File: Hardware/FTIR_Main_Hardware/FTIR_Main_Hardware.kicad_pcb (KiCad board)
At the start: 2 copper layers, 63 parts, among them J1 RJ45_LED_Shielded, Q1 IRF7606PBF, Q2 BSS138, Q3 IRF7606PBF, Q4 IRF7606PBF, Q5 BSS138, Q6 BSS138, U1 Opamp_Dual, U2 D36V28F7, U3 OKI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

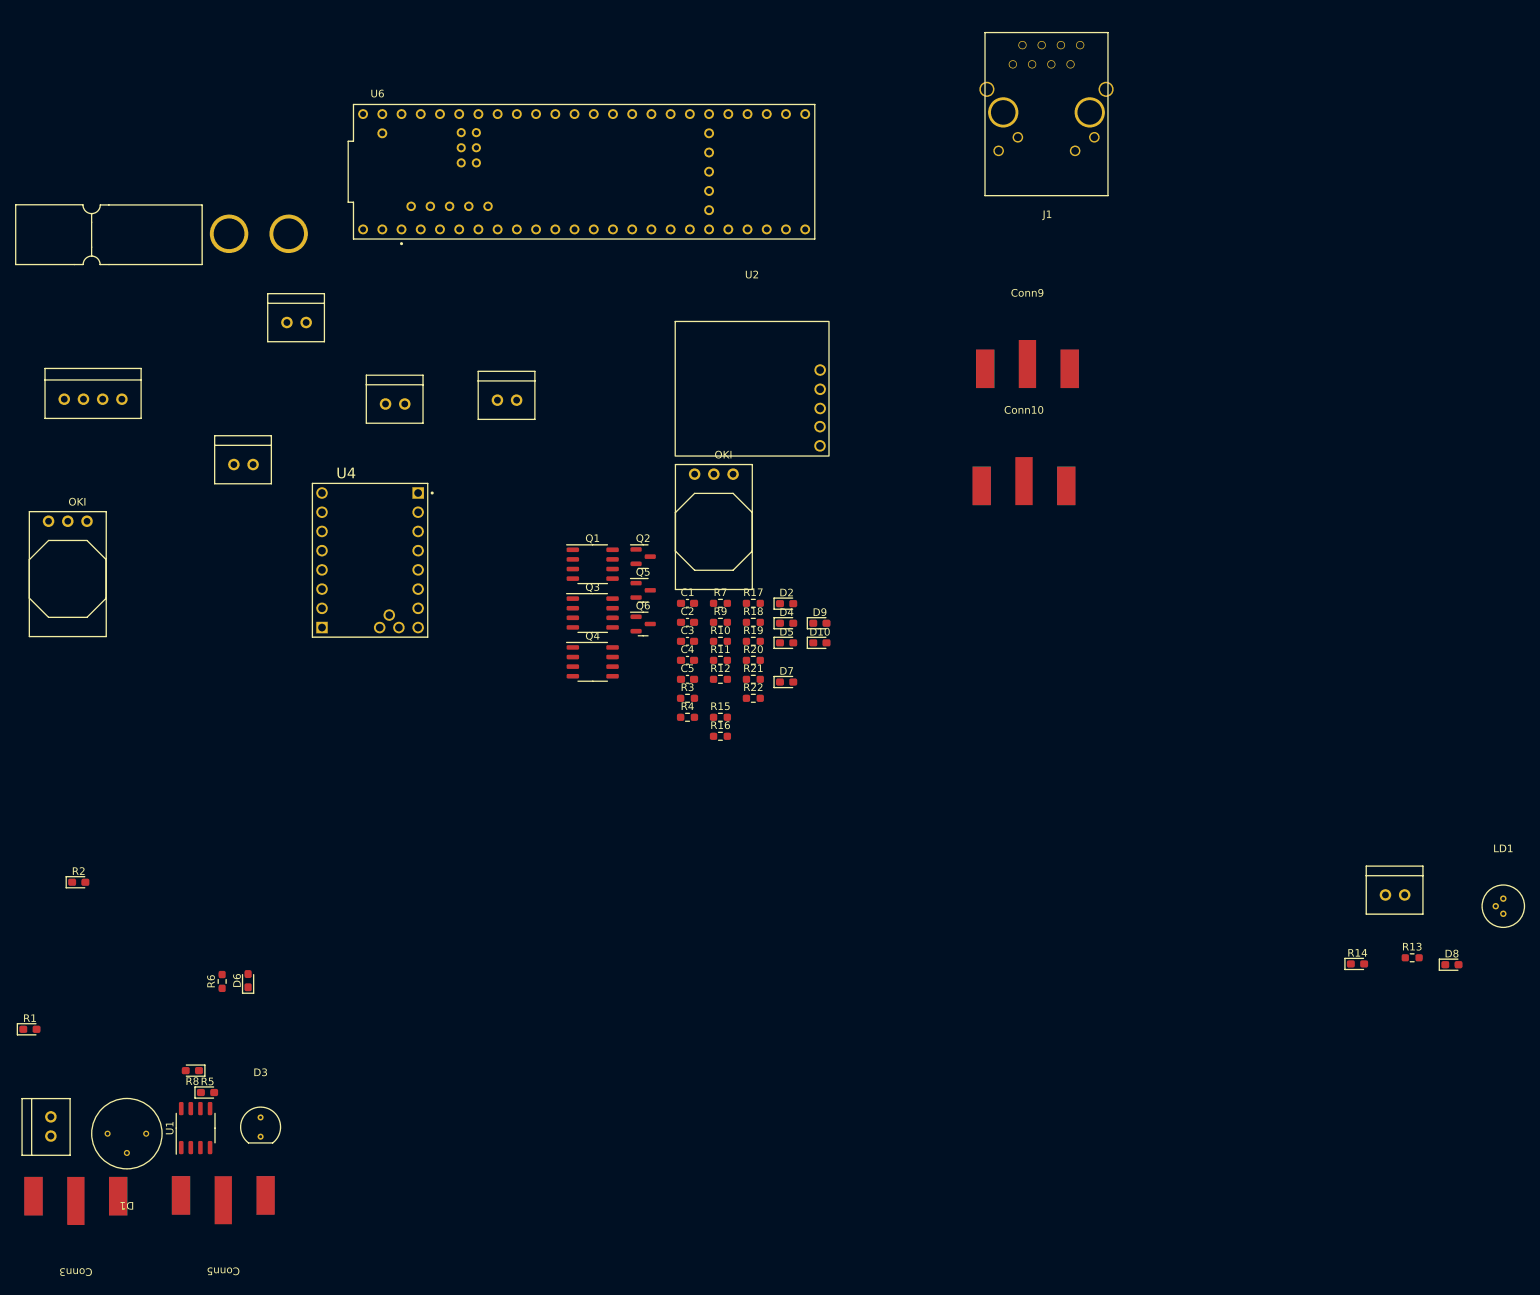
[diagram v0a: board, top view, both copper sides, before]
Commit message: updating footprint libraries
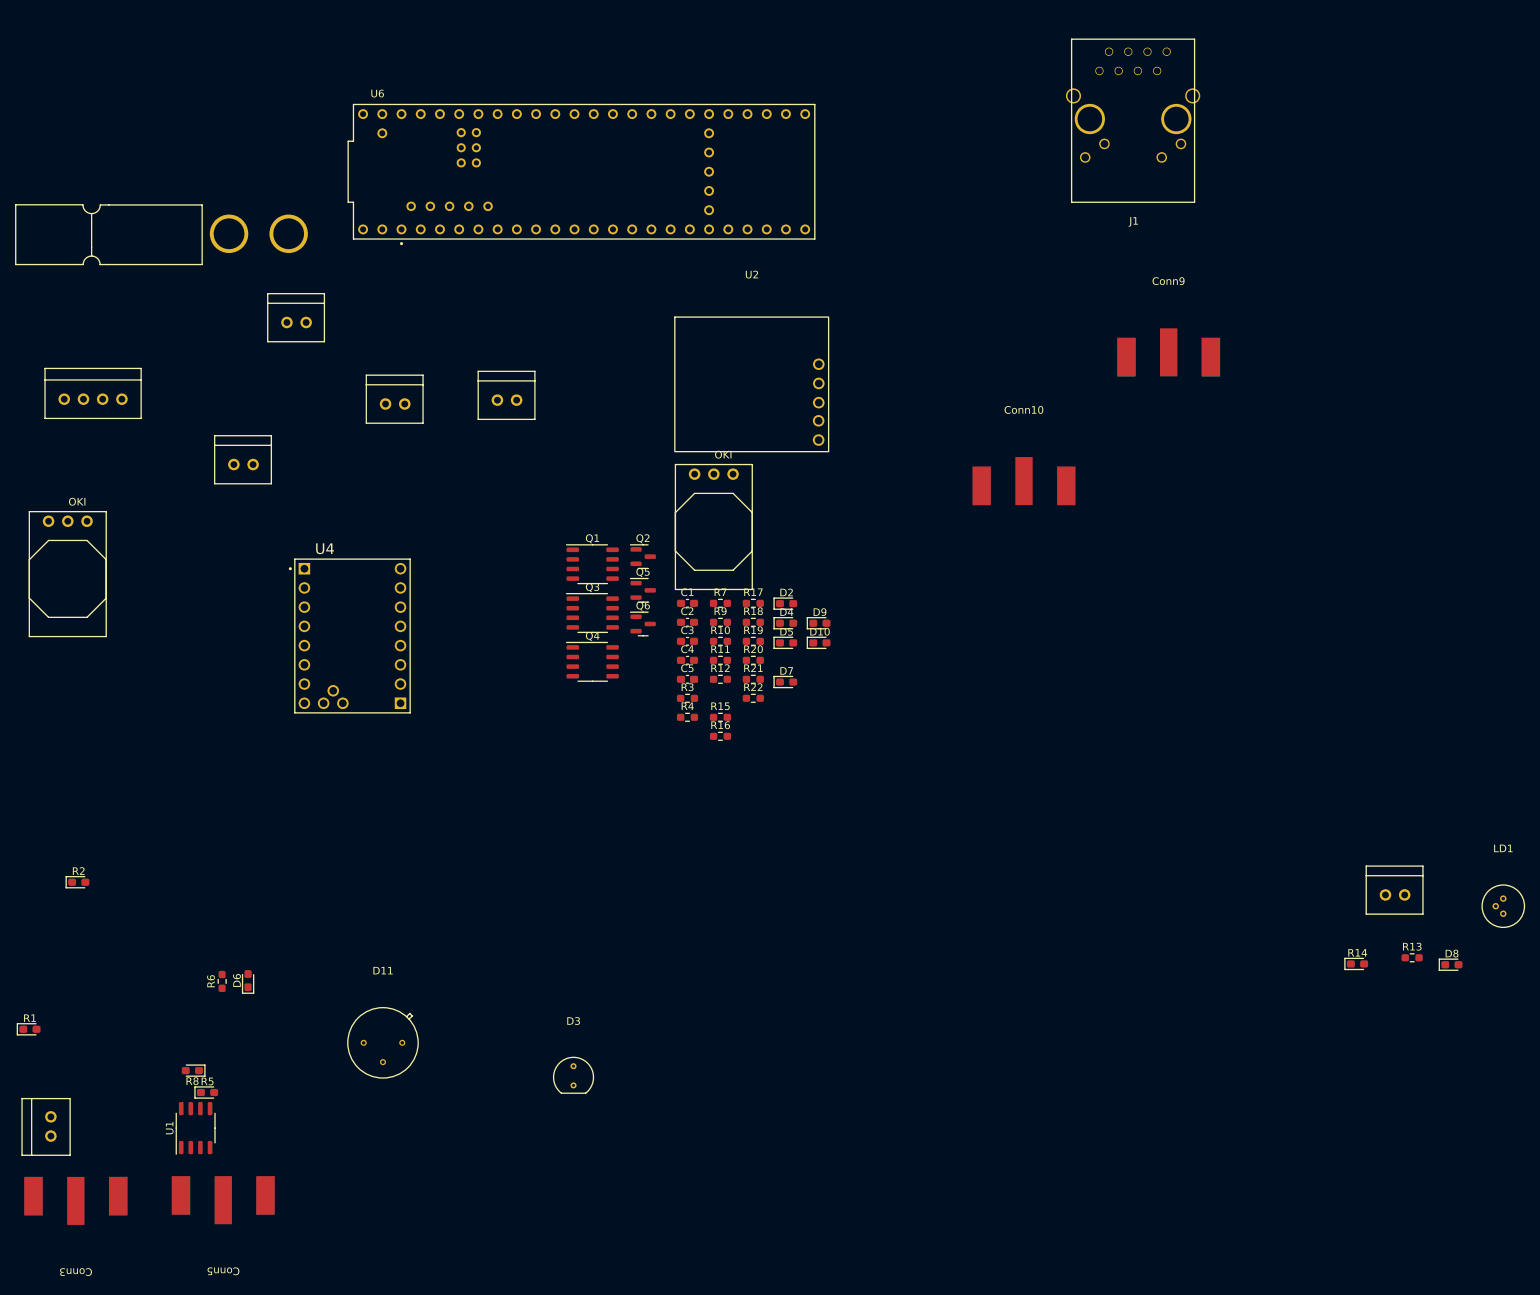
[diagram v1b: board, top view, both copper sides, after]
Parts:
- removed D1: D_Photo, FTIR_Footprints:P16113-011MN
- added D11: S5971, FTIR_Footprints:P16113-011MN, F.Cu at (106.2, 156.0)
- moved D3 41.9 mm to (131.4, 160.4)
- moved Conn9 18.7 mm to (210.0, 65.4)
- moved J1 11.5 mm to (205.4, 46.9)
- moved U4 10.4 mm to (101.7, 102.2)

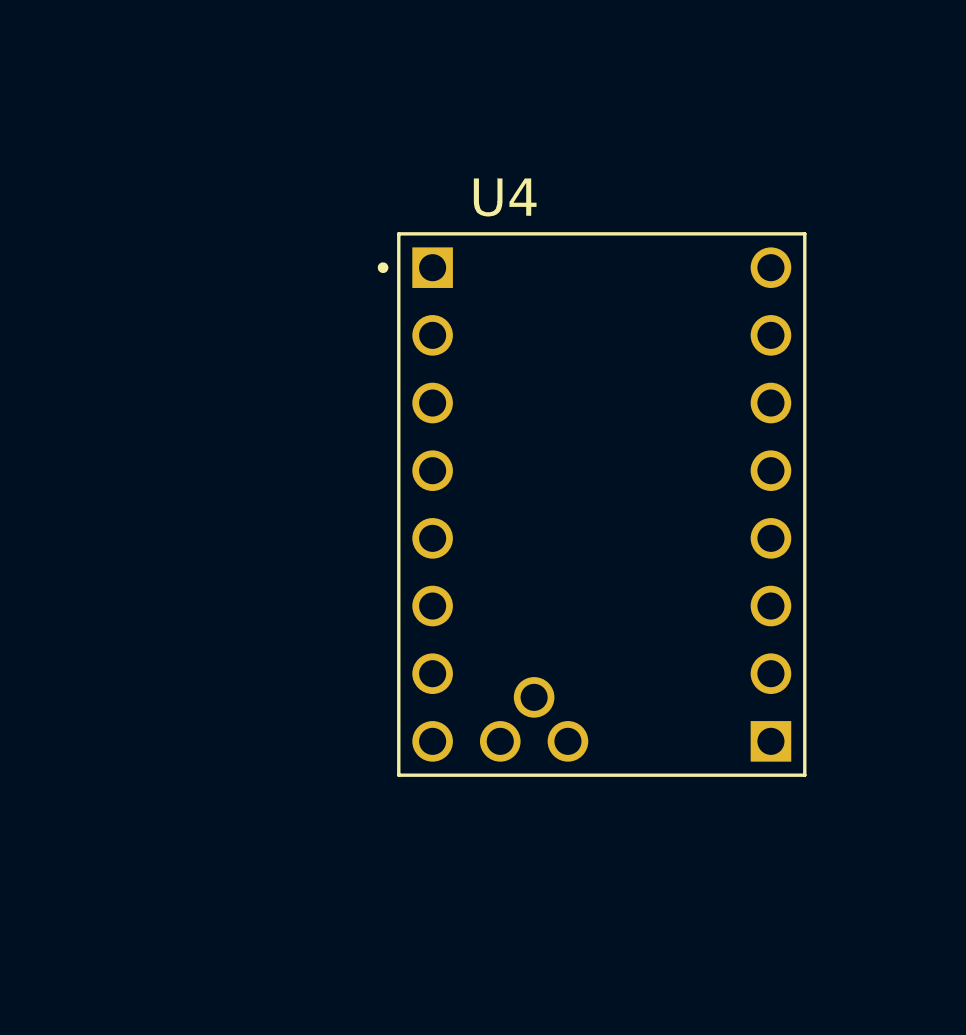
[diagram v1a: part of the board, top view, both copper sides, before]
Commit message: Matched pin numbers between footprints and symbols
cursed
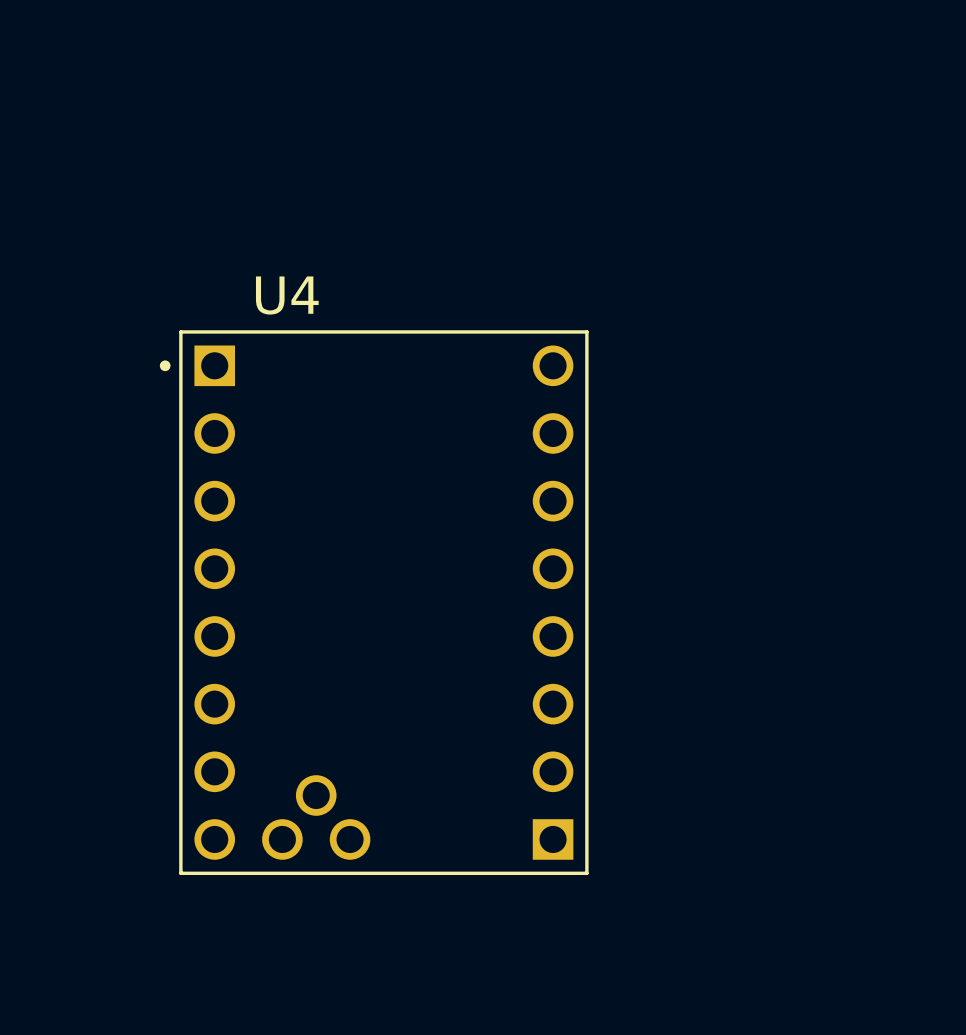
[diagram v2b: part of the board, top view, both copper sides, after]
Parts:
- moved U4 8.97 mm to (93.5, 105.9)
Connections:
- Conn4 pad 1: Net-(U4-M2B) -> Net-(Conn4-Pad1)
- Conn4 pad 2: Net-(U4-M2A) -> Net-(Conn4-Pad2)
- Conn4 pad 3: Net-(U4-M1A) -> Net-(Conn4-Pad3)
- Conn4 pad 4: Net-(U4-M1B) -> Net-(Conn4-Pad4)
- U4 pad CLK: (no net) -> unconnected-(U4-PadCLK)
- U4 pad DIR: (no net) -> DIR
- U4 pad EN: (no net) -> DRIVER_EN
- U4 pad GND: (no net) -> GND
- U4 pad M1A: (no net) -> Net-(Conn4-Pad2)
- U4 pad M1B: (no net) -> Net-(Conn4-Pad1)
- U4 pad M2A: (no net) -> Net-(Conn4-Pad3)
- U4 pad M2B: (no net) -> Net-(Conn4-Pad4)
- U4 pad MS1: (no net) -> MS1_CTRL
- U4 pad MS2: (no net) -> MS2_CTRL
- U4 pad PDN: (no net) -> unconnected-(U4-PadPDN)
- U4 pad STEP: (no net) -> STEP
- U4 pad UART: (no net) -> GND
- U4 pad VIO: (no net) -> +3V3
- U4 pad VM: (no net) -> +7.5V
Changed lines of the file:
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@@
   (net 4 "Net-(C3-Pad1)")
   (net 5 "+3V3")
-  (net 6 "Net-(U4-M1B)")
-  (net 7 "Net-(U4-M1A)")
-  (net 8 "Net-(U4-M2A)")
-  (net 9 "Net-(U4-M2B)")
+  (net 6 "Net-(Conn4-Pad1)")
+  (net 7 "Net-(Conn4-Pad2)")
+  (net 8 "Net-(Conn4-Pad3)")
+  (net 9 "Net-(Conn4-Pad4)")
   (net 10 "Net-(Conn6-Pad1)")
   (net 11 "Net-(U6-A0)")
@@
   (net 91 "unconnected-(U6-PadVBAT)")
   (net 92 "unconnected-(U6-PadVUSB)")
+  (net 93 "unconnected-(U4-PadCLK)")
+  (net 94 "unconnected-(U4-PadPDN)")
   (footprint "Package_TO_SOT_SMD:SOT-23" (layer "F.Cu")
     (at 140.5708 96.1982)
@@
   )
   (footprint "FTIR_Footprints:MODULE_TMC2208_SILENTSTEPSTICK" (layer "F.Cu")
-    (at 101.6588 102.235)
+    (at 93.48 105.918)
     (property "Sheetfile" "FTIR_Main_Hardware.kicad_sch")
     (property "Sheetname" "")
@@
       (stroke (width 0.2) (type solid)) (fill none) (layer "F.Fab"))
     (pad "CLK" thru_hole circle (at -5.85 -3.81) (size 1.524 1.524) (drill 1.016) (layers "*.Cu" "*.Mask")
-      (solder_mask_margin 0.102))
+      (net 93 "unconnected-(U4-PadCLK)") (pinfunction "CLK") (pintype "input+no_connect") (solder_mask_margin 0.102))
     (pad "DIAG" thru_hole circle (at -2.04 7.239) (size 1.524 1.524) (drill 1.016) (layers "*.Cu" "*.Mask")
       (solder_mask_margin 0.102))
     (pad "DIR" thru_hole rect (at -5.85 -8.89) (size 1.524 1.524) (drill 1.016) (layers "*.Cu" "*.Mask")
-      (solder_mask_margin 0.102))
+      (net 65 "DIR") (pinfunction "DIR") (pintype "input") (solder_mask_margin 0.102))
     (pad "EN" thru_hole circle (at -5.85 8.89) (size 1.524 1.524) (drill 1.016) (layers "*.Cu" "*.Mask")
-      (solder_mask_margin 0.102))
+      (net 63 "DRIVER_EN") (pinfunction "EN") (pintype "input") (solder_mask_margin 0.102))
     (pad "GND" thru_hole circle (at 6.85 -8.89) (size 1.524 1.524) (drill 1.016) (layers "*.Cu" "*.Mask")
-      (solder_mask_margin 0.102))
+      (net 2 "GND") (pinfunction "GND") (pintype "input") (solder_mask_margin 0.102))
     (pad "GND" thru_hole circle (at 6.85 6.35) (size 1.524 1.524) (drill 1.016) (layers "*.Cu" "*.Mask")
-      (solder_mask_margin 0.102))
+      (net 2 "GND") (pinfunction "GND") (pintype "input") (solder_mask_margin 0.102))
     (pad "INDEX" thru_hole circle (at -0.77 8.89) (size 1.524 1.524) (drill 1.016) (layers "*.Cu" "*.Mask")
       (solder_mask_margin 0.102))
     (pad "M1A" thru_hole circle (at 6.85 -1.27) (size 1.524 1.524) (drill 1.016) (layers "*.Cu" "*.Mask")
-      (solder_mask_margin 0.102))
+      (net 7 "Net-(Conn4-Pad2)") (pinfunction "M1A") (pintype "input") (solder_mask_margin 0.102))
     (pad "M1B" thru_hole circle (at 6.85 -3.81) (size 1.524 1.524) (drill 1.016) (layers "*.Cu" "*.Mask")
-      (solder_mask_margin 0.102))
+      (net 6 "Net-(Conn4-Pad1)") (pinfunction "M1B") (pintype "input") (solder_mask_margin 0.102))
     (pad "M2A" thru_hole circle (at 6.85 1.27) (size 1.524 1.524) (drill 1.016) (layers "*.Cu" "*.Mask")
-      (solder_mask_margin 0.102))
+      (net 8 "Net-(Conn4-Pad3)") (pinfunction "M2A") (pintype "input") (solder_mask_margin 0.102))
     (pad "M2B" thru_hole circle (at 6.85 3.81) (size 1.524 1.524) (drill 1.016) (layers "*.Cu" "*.Mask")
-      (solder_mask_margin 0.102))
+      (net 9 "Net-(Conn4-Pad4)") (pinfunction "M2B") (pintype "input") (solder_mask_margin 0.102))
     (pad "MS1" thru_hole circle (at -5.85 6.35) (size 1.524 1.524) (drill 1.016) (layers "*.Cu" "*.Mask")
-      (solder_mask_margin 0.102))
+      (net 48 "MS1_CTRL") (pinfunction "MS1") (pintype "input") (solder_mask_margin 0.102))
     (pad "MS2" thru_hole circle (at -5.85 3.81) (size 1.524 1.524) (drill 1.016) (layers "*.Cu" "*.Mask")
-      (solder_mask_margin 0.102))
+      (net 49 "MS2_CTRL") (pinfunction "MS2") (pintype "input") (solder_mask_margin 0.102))
     (pad "PDN" thru_hole circle (at -5.85 -1.27) (size 1.524 1.524) (drill 1.016) (layers "*.Cu" "*.Mask")
-      (solder_mask_margin 0.102))
+      (net 94 "unconnected-(U4-PadPDN)") (pinfunction "PDN") (pintype "input+no_connect") (solder_mask_margin 0.102))
     (pad "STEP" thru_hole circle (at -5.85 -6.35) (size 1.524 1.524) (drill 1.016) (layers "*.Cu" "*.Mask")
-      (solder_mask_margin 0.102))
+      (net 64 "STEP") (pinfunction "STEP") (pintype "input") (solder_mask_margin 0.102))
     (pad "UART" thru_hole circle (at -5.85 1.27) (size 1.524 1.524) (drill 1.016) (layers "*.Cu" "*.Mask")
-      (solder_mask_margin 0.102))
+      (net 2 "GND") (pinfunction "UART") (pintype "input") (solder_mask_margin 0.102))
     (pad "VIO" thru_hole circle (at 6.85 -6.35) (size 1.524 1.524) (drill 1.016) (layers "*.Cu" "*.Mask")
-      (solder_mask_margin 0.102))
+      (net 5 "+3V3") (pinfunction "VIO") (pintype "input") (solder_mask_margin 0.102))
     (pad "VM" thru_hole rect (at 6.85 8.89) (size 1.524 1.524) (drill 1.016) (layers "*.Cu" "*.Mask")
-      (solder_mask_margin 0.102))
+      (net 44 "+7.5V") (pinfunction "VM") (pintype "input") (solder_mask_margin 0.102))
     (pad "VREF" thru_hole circle (at -3.31 8.89) (size 1.524 1.524) (drill 1.016) (layers "*.Cu" "*.Mask")
       (solder_mask_margin 0.102))
@@
       (stroke (width 0.15) (type solid)) (layer "F.SilkS"))
     (pad "1" thru_hole circle (at 0 0) (size 1.524 1.524) (drill 0.9) (layers "*.Cu" "*.Mask")
-      (net 9 "Net-(U4-M2B)") (pintype "input"))
+      (net 6 "Net-(Conn4-Pad1)") (pintype "input"))
     (pad "2" thru_hole circle (at 2.54 0) (size 1.524 1.524) (drill 0.9) (layers "*.Cu" "*.Mask")
-      (net 8 "Net-(U4-M2A)") (pintype "input"))
+      (net 7 "Net-(Conn4-Pad2)") (pintype "input"))
     (pad "3" thru_hole circle (at 5.08 0) (size 1.524 1.524) (drill 0.9) (layers "*.Cu" "*.Mask")
-      (net 7 "Net-(U4-M1A)") (pintype "input"))
+      (net 8 "Net-(Conn4-Pad3)") (pintype "input"))
     (pad "4" thru_hole circle (at 7.62 0) (size 1.524 1.524) (drill 0.9) (layers "*.Cu" "*.Mask")
-      (net 6 "Net-(U4-M1B)") (pintype "input"))
+      (net 9 "Net-(Conn4-Pad4)") (pintype "input"))
     (pad "4" thru_hole circle (at 7.62 0) (size 1.524 1.524) (drill 0.9) (layers "*.Cu" "*.Mask")
-      (net 6 "Net-(U4-M1B)") (pintype "input"))
+      (net 9 "Net-(Conn4-Pad4)") (pintype "input"))
     (model "${MRDT_KICAD_LIBRARIES}/3D Files/MRDT_Connctors/Molex_SL_04_Vertical.stp"
       (offset (xyz -2.539999962 -2.539999962 13.3349998))
